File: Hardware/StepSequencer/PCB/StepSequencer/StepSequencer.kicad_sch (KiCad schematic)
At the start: 69 parts, among them J1 Conn_01x04_Male, SW1 SW_DIP_x01, SW10 SW_DIP_x01, SW11 SW_DIP_x01, SW12 SW_DIP_x01, SW13 SW_DIP_x01, SW14 SW_DIP_x01, SW15 SW_DIP_x01, SW16 SW_DIP_x01, SW17 SW_DIP_x01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

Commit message: General refactoring
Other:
- title: Daisy Seed Development Kit Step Sequencer Interface -> Daisy Seed Development Kit Step Sequencer
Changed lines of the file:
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@@
   (paper "A4")
   (title_block
-    (title "Daisy Seed Development Kit Step Sequencer Interface")
+    (title "Daisy Seed Development Kit Step Sequencer")
     (date "2024-01-22")
     (rev "2.0")

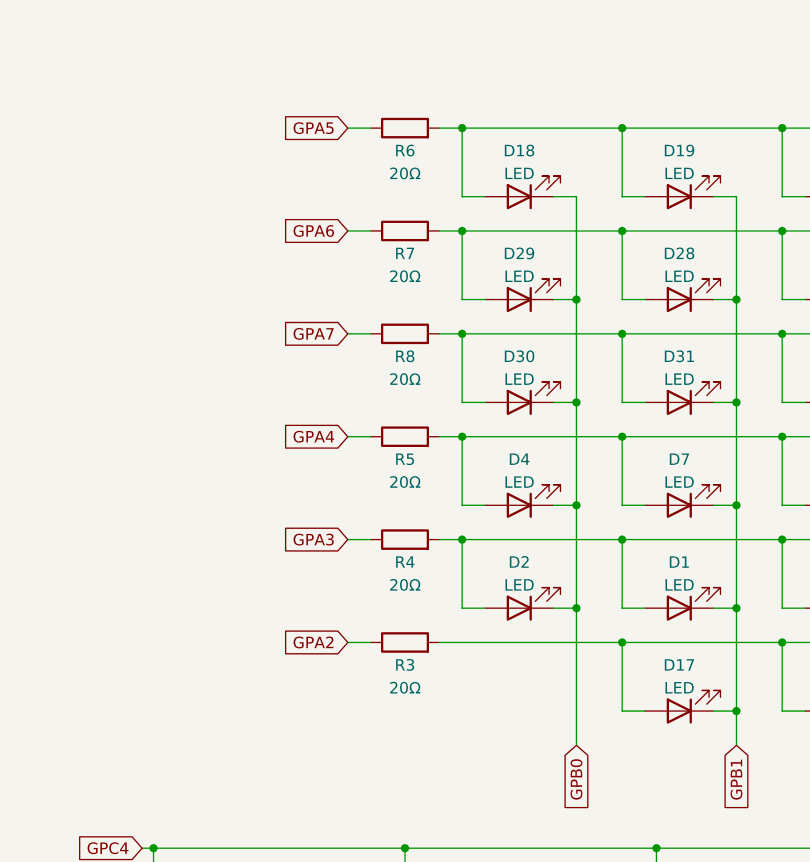
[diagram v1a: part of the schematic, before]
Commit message: Configured drivers to new hardware
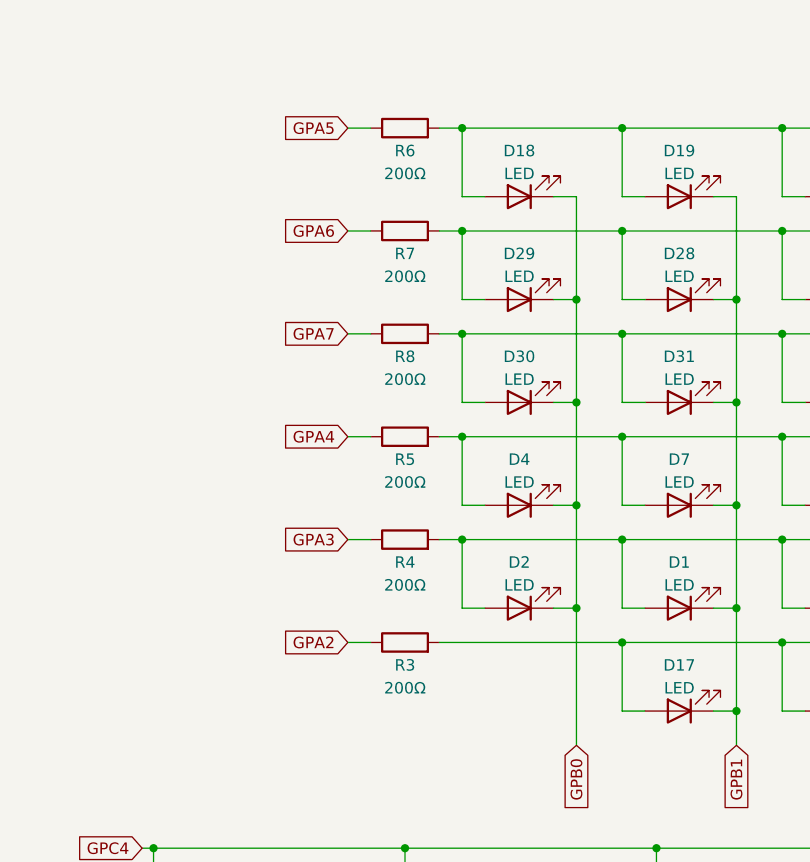
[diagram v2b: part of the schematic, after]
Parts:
- R3, R4, R5, R6, R7, R8: value 20Ω -> 200Ω
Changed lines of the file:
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@@
     (in_bom yes) (on_board yes)
     (property "Reference" "R3" (id 0) (at 147.32 74.93 90))
-    (property "Value" "20Ω" (id 1) (at 147.32 77.47 90))
+    (property "Value" "200Ω" (id 1) (at 147.32 77.47 90))
     (property "Footprint" "Resistor_THT:R_Axial_DIN0207_L6.3mm_D2.5mm_P10.16mm_Horizontal" (id 2) (at 147.32 74.168 90)
       (effects (font (size 1.27 1.27)) hide)
@@
     (in_bom yes) (on_board yes)
     (property "Reference" "R7" (id 0) (at 147.32 29.21 90))
-    (property "Value" "20Ω" (id 1) (at 147.32 31.75 90))
+    (property "Value" "200Ω" (id 1) (at 147.32 31.75 90))
     (property "Footprint" "Resistor_THT:R_Axial_DIN0207_L6.3mm_D2.5mm_P10.16mm_Horizontal" (id 2) (at 147.32 28.448 90)
       (effects (font (size 1.27 1.27)) hide)
@@
     (in_bom yes) (on_board yes)
     (property "Reference" "R6" (id 0) (at 147.32 17.78 90))
-    (property "Value" "20Ω" (id 1) (at 147.32 20.32 90))
+    (property "Value" "200Ω" (id 1) (at 147.32 20.32 90))
     (property "Footprint" "Resistor_THT:R_Axial_DIN0207_L6.3mm_D2.5mm_P10.16mm_Horizontal" (id 2) (at 147.32 17.018 90)
       (effects (font (size 1.27 1.27)) hide)
@@
     (in_bom yes) (on_board yes)
     (property "Reference" "R8" (id 0) (at 147.32 40.64 90))
-    (property "Value" "20Ω" (id 1) (at 147.32 43.18 90))
+    (property "Value" "200Ω" (id 1) (at 147.32 43.18 90))
     (property "Footprint" "Resistor_THT:R_Axial_DIN0207_L6.3mm_D2.5mm_P10.16mm_Horizontal" (id 2) (at 147.32 39.878 90)
       (effects (font (size 1.27 1.27)) hide)
@@
     (in_bom yes) (on_board yes)
     (property "Reference" "R5" (id 0) (at 147.32 52.07 90))
-    (property "Value" "20Ω" (id 1) (at 147.32 54.61 90))
+    (property "Value" "200Ω" (id 1) (at 147.32 54.61 90))
     (property "Footprint" "Resistor_THT:R_Axial_DIN0207_L6.3mm_D2.5mm_P10.16mm_Horizontal" (id 2) (at 147.32 51.308 90)
       (effects (font (size 1.27 1.27)) hide)
@@
     (in_bom yes) (on_board yes)
     (property "Reference" "R4" (id 0) (at 147.32 63.5 90))
-    (property "Value" "20Ω" (id 1) (at 147.32 66.04 90))
+    (property "Value" "200Ω" (id 1) (at 147.32 66.04 90))
     (property "Footprint" "Resistor_THT:R_Axial_DIN0207_L6.3mm_D2.5mm_P10.16mm_Horizontal" (id 2) (at 147.32 62.738 90)
       (effects (font (size 1.27 1.27)) hide)
@@
     )
     (path "/25657383-8d70-421e-947b-1e9ef5f36669"
-      (reference "R3") (unit 1) (value "20Ω") (footprint "Resistor_THT:R_Axial_DIN0207_L6.3mm_D2.5mm_P10.16mm_Horizontal")
+      (reference "R3") (unit 1) (value "200Ω") (footprint "Resistor_THT:R_Axial_DIN0207_L6.3mm_D2.5mm_P10.16mm_Horizontal")
     )
     (path "/e2684644-e6fd-4a2e-9bac-0cd3240a00ed"
-      (reference "R4") (unit 1) (value "20Ω") (footprint "Resistor_THT:R_Axial_DIN0207_L6.3mm_D2.5mm_P10.16mm_Horizontal")
+      (reference "R4") (unit 1) (value "200Ω") (footprint "Resistor_THT:R_Axial_DIN0207_L6.3mm_D2.5mm_P10.16mm_Horizontal")
     )
     (path "/badeb53d-6596-4ab3-b932-16b933ccc342"
-      (reference "R5") (unit 1) (value "20Ω") (footprint "Resistor_THT:R_Axial_DIN0207_L6.3mm_D2.5mm_P10.16mm_Horizontal")
+      (reference "R5") (unit 1) (value "200Ω") (footprint "Resistor_THT:R_Axial_DIN0207_L6.3mm_D2.5mm_P10.16mm_Horizontal")
     )
     (path "/558b929b-1dda-4b48-9ec0-2b4c8b74780b"
-      (reference "R6") (unit 1) (value "20Ω") (footprint "Resistor_THT:R_Axial_DIN0207_L6.3mm_D2.5mm_P10.16mm_Horizontal")
+      (reference "R6") (unit 1) (value "200Ω") (footprint "Resistor_THT:R_Axial_DIN0207_L6.3mm_D2.5mm_P10.16mm_Horizontal")
     )
     (path "/28581666-3178-49b2-8301-906fddf820eb"
-      (reference "R7") (unit 1) (value "20Ω") (footprint "Resistor_THT:R_Axial_DIN0207_L6.3mm_D2.5mm_P10.16mm_Horizontal")
+      (reference "R7") (unit 1) (value "200Ω") (footprint "Resistor_THT:R_Axial_DIN0207_L6.3mm_D2.5mm_P10.16mm_Horizontal")
     )
     (path "/7dc1f626-8232-4d5e-a872-237bffc0e611"
-      (reference "R8") (unit 1) (value "20Ω") (footprint "Resistor_THT:R_Axial_DIN0207_L6.3mm_D2.5mm_P10.16mm_Horizontal")
+      (reference "R8") (unit 1) (value "200Ω") (footprint "Resistor_THT:R_Axial_DIN0207_L6.3mm_D2.5mm_P10.16mm_Horizontal")
     )
     (path "/502ec8d5-f7e6-4010-af11-c6758948891a"
